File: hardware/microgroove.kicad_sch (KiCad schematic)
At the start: 22 parts, among them J1 UJ2-MIBH-4-SMT-TR, J2 SJ1-3513, J3 SJ1-3513, SW1 RotaryEncoder, SW10 SW_Push_Dual, SW11 SW_Push_Dual, SW2 RotaryEncoder, SW3 RotaryEncoder, SW4 RotaryEncoder, SW5 RotaryEncoder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

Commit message: Add custom KiCAD symbol for the NHD-2.7-12864WDW3 2.7in OLED display
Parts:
- removed DS1: NHD-2.7-12864WDW3-M, NHD-2.7-12864WDW3-M:NHD2712864WDW3-M, symbol NHD-2.7-12864WDW3-M:NHD-2.7-12864WDW3-M
- added DS1: NHD-2.7-12864WDW3, symbol NHD-2.7-12864WDW3:NHD-2.7-12864WDW3
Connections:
- net +3V3: now also DS1.16 (~{RES}), DS1.2 (VDD)
- net GND: now also DS1.1 (VSS), DS1.10 (VSS), DS1.11 (VSS), DS1.12 (VSS), DS1.13 (VSS), DS1.14 (VSS), DS1.19 (BS1), DS1.20 (BS0), DS1.5 (VSS), DS1.6 (VSS)
- net at SW8.3: no longer U1.22 (GPIO17)
- net at SW7.1: now also U1.29 (GPIO22)
- net at SW7.3: no longer U1.21 (GPIO16)
- net at SW9.1: now also U1.21 (GPIO16)
- net at U1.24 (GPIO18): now also DS1.7 (SCLK); no longer SW9.3
- net at SW11.1: now also U1.19 (GPIO14)
- net at SW11.3: no longer U1.26 (GPIO20)
- net at SW10.1: now also U1.20 (GPIO15)
- net at U1.25 (GPIO19): now also DS1.8 (SDIN); no longer SW10.3
- net at U1.27 (GPIO21): now also DS1.17 (~{CS})
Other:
- moved on the sheet: SW1, SW10, SW11, SW2, SW3, SW4, SW5, SW6, SW7, SW8, SW9

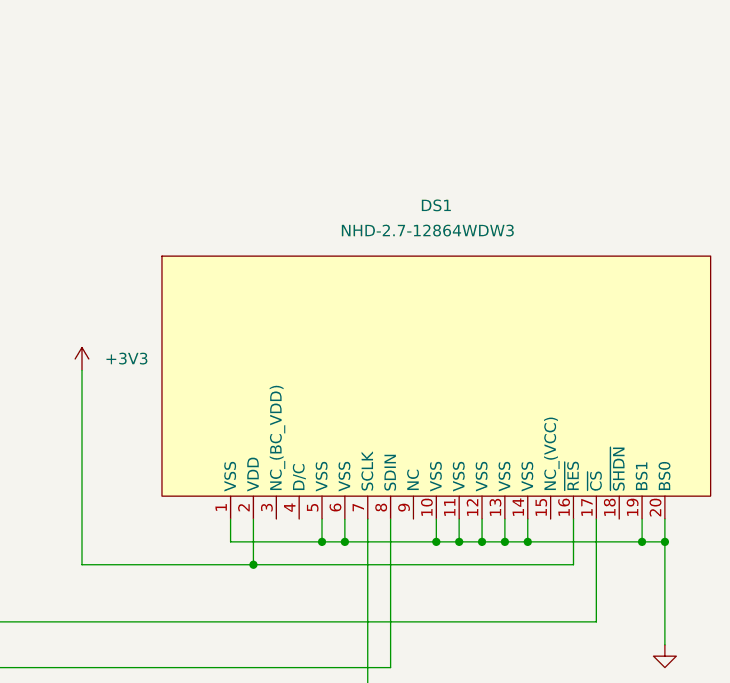
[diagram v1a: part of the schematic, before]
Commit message: Add KiCAD symbol and footprint for NHD-2.7-12864WDW3 from Mouser
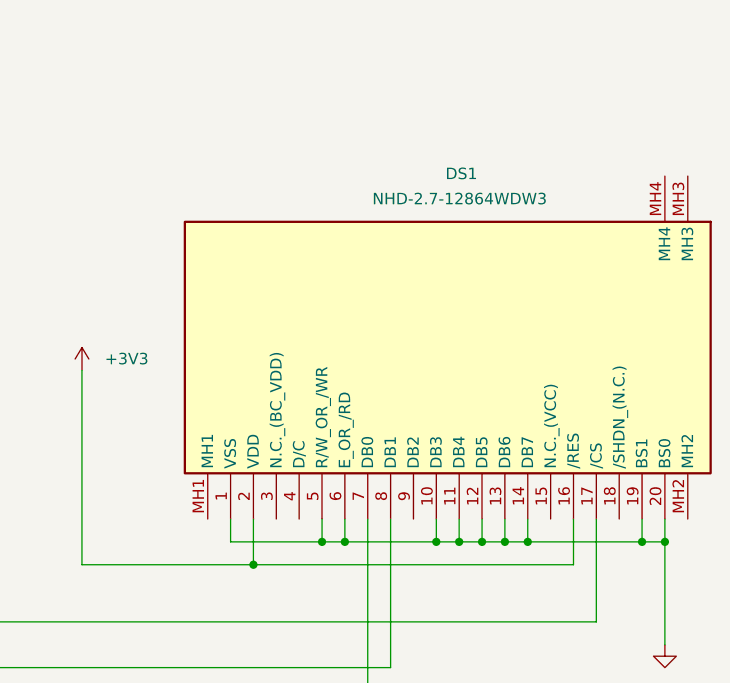
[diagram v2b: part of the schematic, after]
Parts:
- DS1: footprint (none) -> NHD2712864WDW3; Height (none) -> 6; Manufacturer_Name (none) -> Newhaven Display; Manufacturer_Part_Number (none) -> NHD-2.7-12864WDW3; Mouser Part Number (none) -> 763-NHD2712864WDW3; Mouser Price/Stock (none) -> https://www.mouser.co.uk/ProductDetail/Newhaven-Display/NHD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
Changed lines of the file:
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@@
 	(symbol
 		(lib_id "NHD-2.7-12864WDW3:NHD-2.7-12864WDW3")
-		(at 218.44 81.28 0)
+		(at 246.38 58.42 270)
 		(unit 1)
 		(exclude_from_sim no)
@@
 		(dnp no)
 		(property "Reference" "DS1"
-			(at 216.662 61.722 0)
+			(at 219.456 58.166 90)
 			(effects
 				(font
@@
 		)
 		(property "Value" "NHD-2.7-12864WDW3"
-			(at 207.772 64.516 0)
+			(at 211.328 60.96 90)
 			(effects
 				(font
@@
 			)
 		)
-		(property "Footprint" ""
-			(at 218.44 81.28 0)
+		(property "Footprint" "NHD2712864WDW3"
+			(at 246.38 58.42 0)
 			(effects
 				(font
@@
 			)
 		)
-		(property "Datasheet" ""
-			(at 218.44 81.28 0)
+		(property "Datasheet" "https://componentsearchengine.com/Datasheets/1/NHD-2.7-12864WDW3.pdf"
+			(at 246.38 58.42 0)
 			(effects
 				(font
@@
 			)
 		)
-		(property "Description" ""
-			(at 218.44 81.28 0)
+		(property "Description" "LCD OLED GRAPHIC 128X64 WHT"
+			(at 246.38 58.42 0)
 			(effects
 				(font
 					(size 1.27 1.27)
 				)
+				(hide yes)
+			)
+		)
+		(property "Height" "6"
+			(at -148.54 92.71 0)
+			(effects
+				(font
+					(size 1.27 1.27)
+				)
+				(justify left top)
+				(hide yes)
+			)
+		)
+		(property "Mouser Part Number" "763-NHD2712864WDW3"
+			(at -248.54 92.71 0)
+			(effects
+				(font
+					(size 1.27 1.27)
+				)
+				(justify left top)
+				(hide yes)
+			)
+		)
+		(property "Mouser Price/Stock" "https://www.mouser.co.uk/ProductDetail/Newhaven-Display/NHD-2.7-12864WDW3?qs=EU6FO9ffTwf2tAy5%2FRPmRA%3D%3D"
+			(at -348.54 92.71 0)
+			(effects
+				(font
+					(size 1.27 1.27)
+				)
+				(justify left top)
+				(hide yes)
+			)
+		)
+		(property "Manufacturer_Name" "Newhaven Display"
+			(at -448.54 92.71 0)
+			(effects
+				(font
+					(size 1.27 1.27)
+				)
+				(justify left top)
+				(hide yes)
+			)
+		)
+		(property "Manufacturer_Part_Number" "NHD-2.7-12864WDW3"
+			(at -548.54 92.71 0)
+			(effects
+				(font
+					(size 1.27 1.27)
+				)
+				(justify left top)
 				(hide yes)
 			)
@@
 		(pin "16"
 		)
+		(pin "MH1"
+		)
+		(pin "MH2"
+		)
+		(pin "MH3"
+		)
+		(pin "MH4"
+		)
 		(instances

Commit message: Assign footprints for KiCAD schematic symbols
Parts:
- removed SW10, SW11, SW7, SW8, SW9: SW_Push_Dual, symbol Switch:SW_Push_Dual
- added SW10, SW11, SW7, SW8, SW9: TL1100F160Q6JBLK, footprints:SW4_TL1100F160Q6JBLK_EWI, symbol SW4_TL1100F160Q6JBLK_EWI:TL1100F160Q6JBLK
- DS1: footprint NHD2712864WDW3 -> NHD-2.7-12864WDW3:NHD2712864WDW3
- J1: footprint CUIDEVICES_UJ2-MIBH-4-SMT-TR -> UJ2-MIBH-4-SMT-TR:CUIDEVICES_UJ2-MIBH-4-SMT-TR
- J2, J3: footprint SJ1-3513:CUI_SJ1-3513 -> SJ1_3513:CUI_SJ1-3513
- R1, R2, R3, R4: footprint (none) -> Resistor_THT:R_Axial_DIN0207_L6.3mm_D2.5mm_P10.16mm_Horizontal
- SW1, SW2, SW3, SW4, SW5, SW6: footprint (none) -> PEC11R_4215F_S0024:XDCR_PEC11R-4215F-S0024
- U1: footprint RPi_Pico:RPi_Pico_SMD_TH -> MCU_RaspberryPi_and_Boards:RPi_Pico_SMD_TH
- U2: footprint (none) -> Package_DIP:DIP-6_W7.62mm
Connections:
- net GND: now also SW10.2, SW11.2, SW7.2, SW8.2, SW9.2
- net at U1.29 (GPIO22): now also SW7.1
- net at U1.21 (GPIO16): now also SW9.1
- net at U1.19 (GPIO14): now also SW11.1
- net at U1.20 (GPIO15): now also SW10.1
- net at U1.22 (GPIO17): now also SW8.1
